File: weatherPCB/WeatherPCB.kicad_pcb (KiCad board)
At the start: 2 copper layers, 14 parts, among them Q1 2N4403-ND, Q2 2N4401-ND, SW1 SW_Push, SW2 SW_SPDT, U1 PIR_MTN_SNR, U2 WeMos_mini, U3 TFTLCD_ST7735R

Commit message: created pcb
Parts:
- C1: footprint Capacitors_THT:C_Axial_L3.8mm_D2.6mm_P7.50mm_Horizontal -> Capacitors_THT:C_Disc_D3.8mm_W2.6mm_P2.50mm
- moved R5 26.9 mm to (166.0, 139.7), turned to 0 degrees
- moved C1 21.2 mm to (168.9, 133.8), turned to 90 degrees
- moved R2 18.8 mm to (165.5, 132.0), turned to 270 degrees
- moved R1 18.2 mm to (153.5, 126.2), turned to 0 degrees
- moved U1 15.8 mm to (175.2, 135.3)
- moved U3 15.6 mm to (182.9, 92.2)
- moved R6 15.4 mm to (172.0, 135.9), turned to 90 degrees
- moved SW1 12.7 mm to (152.1, 135.6)
- moved U2 11.4 mm to (174.9, 116.5)
- moved R3 10.8 mm to (160.8, 126.2)
- moved Q1 9.48 mm to (160.0, 130.4)
- moved Q2 9.48 mm to (153.7, 130.4)
- moved SW2 6.08 mm to (170.8, 127.0)
- moved R4 2.40 mm to (161.8, 140.5)
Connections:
- U1 pad 1: +3V3 -> GND
- U1 pad 3: GND -> +3V3
- U2 pad 1: +5V -> (no net)
- U2 pad 10: Net-(C1-Pad1) -> GND
- U2 pad 11: Net-(U2-Pad11) -> (no net)
- U2 pad 12: Net-(U2-Pad12) -> Net-(R1-Pad2)
- U2 pad 13: Net-(U2-Pad13) -> Net-(U1-Pad2)
- U2 pad 14: Net-(U2-Pad14) -> Net-(R4-Pad1)
- U2 pad 15: Net-(U2-Pad15) -> (no net)
- U2 pad 16: +3V3 -> (no net)
- U2 pad 2: GND -> Net-(C1-Pad1)
- U2 pad 3: (no net) -> Net-(U2-Pad3)
- U2 pad 4: Net-(R1-Pad2) -> Net-(U2-Pad4)
- U2 pad 5: Net-(U1-Pad2) -> Net-(U2-Pad5)
- U2 pad 6: Net-(R4-Pad1) -> Net-(U2-Pad6)
- U2 pad 7: (no net) -> Net-(U2-Pad7)
- U2 pad 8: (no net) -> +3V3
- U2 pad 9: (no net) -> +5V
- U3 pad 10: Net-(U2-Pad15) -> Net-(U2-Pad7)
- U3 pad 6: Net-(U2-Pad13) -> Net-(U2-Pad5)
- U3 pad 7: Net-(U2-Pad11) -> Net-(U2-Pad3)
- U3 pad 8: Net-(U2-Pad14) -> Net-(U2-Pad6)
- U3 pad 9: Net-(U2-Pad12) -> Net-(U2-Pad4)
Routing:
- net Net-(U1-Pad2): track 0.00 -> 50.9 mm
- net +3V3: track 0.00 -> 44.8 mm, vias 0 -> 2
- net Net-(R4-Pad1): track 0.00 -> 43.1 mm
- net Net-(C1-Pad1): track 0.00 -> 37.1 mm
- net +5V: track 0.00 -> 35.0 mm
- net Net-(R1-Pad2): track 0.00 -> 23.3 mm, vias 0 -> 1
- net Net-(U2-Pad7): track 0.00 -> 18.0 mm, vias 0 -> 1
- net Net-(U2-Pad6): track 0.00 -> 11.9 mm
- net Net-(SW2-Pad2): track 0.00 -> 11.9 mm
- net Net-(Q1-Pad2): track 0.00 -> 10.8 mm
- net Net-(U2-Pad3): track 0.00 -> 9.69 mm
- net Net-(Q1-Pad3): track 0.00 -> 9.64 mm
- net Net-(U2-Pad4): track 0.00 -> 9.52 mm
- net Net-(U2-Pad5): track 0.00 -> 8.64 mm
- net Net-(Q2-Pad2): track 0.00 -> 4.81 mm
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- added copper zone on F.Cu, net +3V3
- added copper zone on B.Cu, net GND
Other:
- board outline added: 35 x 52 mm
- board text added: "Weather Station Miles Young"

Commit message: Rev 1 PCB finished
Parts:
- added H1: MountingHole, Mounting_Holes:MountingHole_2.7mm, F.Cu at (153.0, 93.0)
- added H2: MountingHole, Mounting_Holes:MountingHole_2.7mm, F.Cu at (178.0, 93.0)
- added H3: MountingHole, Mounting_Holes:MountingHole_2.7mm, F.Cu at (153.0, 133.0)
- added H4: MountingHole, Mounting_Holes:MountingHole_2.7mm, F.Cu at (178.0, 133.0)
- C1: footprint Capacitors_THT:C_Disc_D3.8mm_W2.6mm_P2.50mm -> Capacitors_THT:C_Disc_D3.0mm_W1.6mm_P2.50mm
- moved R6 7.42 mm to (166.6, 141.0)
- moved U1 5.82 mm to (169.9, 137.7)
- moved R5 5.75 mm to (161.6, 143.4)
- moved R4 4.88 mm to (161.8, 135.6), turned to 180 degrees
- moved R2 4.20 mm to (164.1, 135.9)
- moved Q2 3.10 mm to (156.8, 130.2)
- moved SW1 2.92 mm to (152.2, 138.5)
- moved Q1 2.34 mm to (162.4, 130.2)
- moved C1 1.92 mm to (167.0, 133.5), turned to 0 degrees
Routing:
- net Net-(R4-Pad1): track 43.1 -> 49.1 mm
- net Net-(U1-Pad2): track 50.9 -> 46.6 mm, vias 0 -> 2
- net Net-(C1-Pad1): track 37.1 -> 41.0 mm
- net +3V3: track 44.8 -> 47.1 mm, vias 2 -> 3
- net Net-(Q2-Pad2): track 4.81 -> 6.85 mm
- net Net-(Q1-Pad3): track 9.64 -> 7.90 mm
- net Net-(R2-Pad2): track 2.84 -> 4.15 mm
- net +5V: track 35.0 -> 34.1 mm
- net Net-(Q1-Pad2): track 10.8 -> 10.3 mm
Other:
- board size 35 x 52 mm -> 35 x 55 mm
- board text added: "JLCJLCJLCJLC"
- board text added: "Weather Station PCB v1 M Young"
- board text removed: "Weather Station Miles Young"

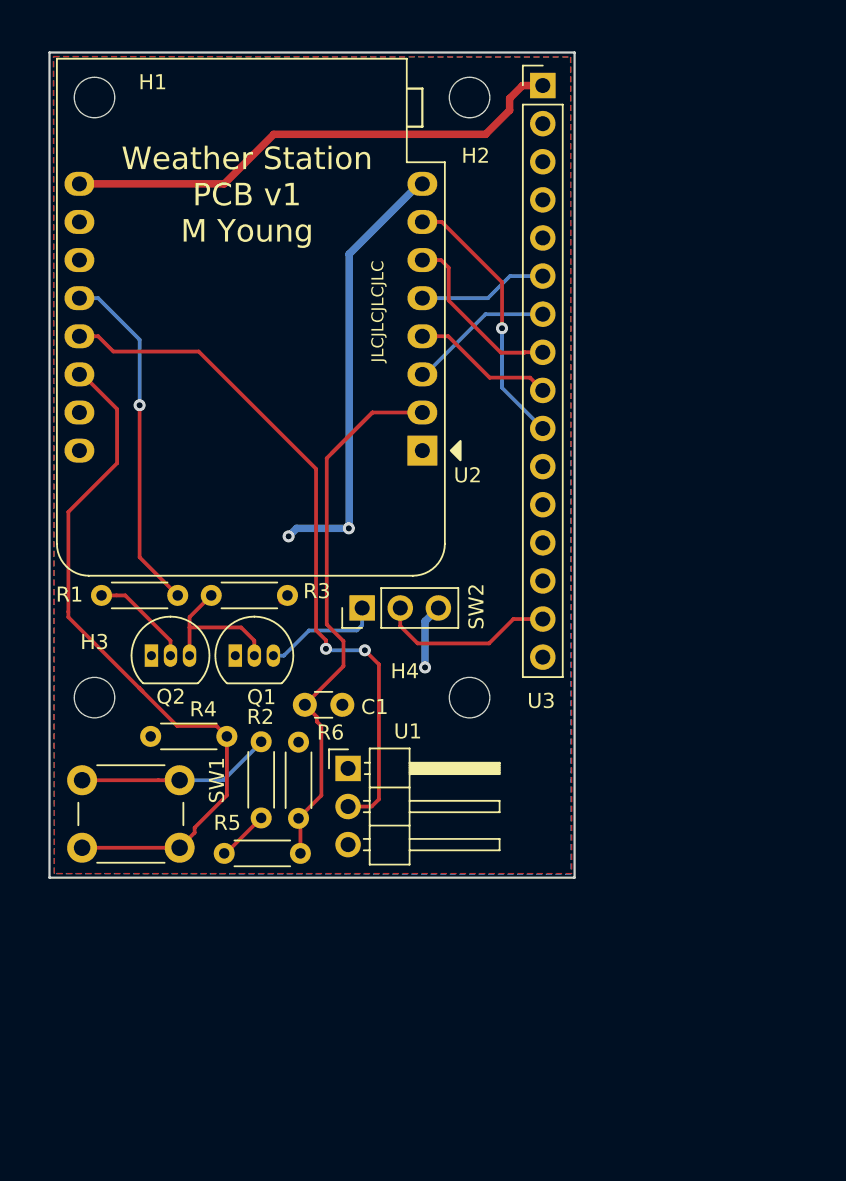
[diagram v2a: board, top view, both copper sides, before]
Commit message: Modified PCB for larger resistor sizes and KiCad error with display wiring
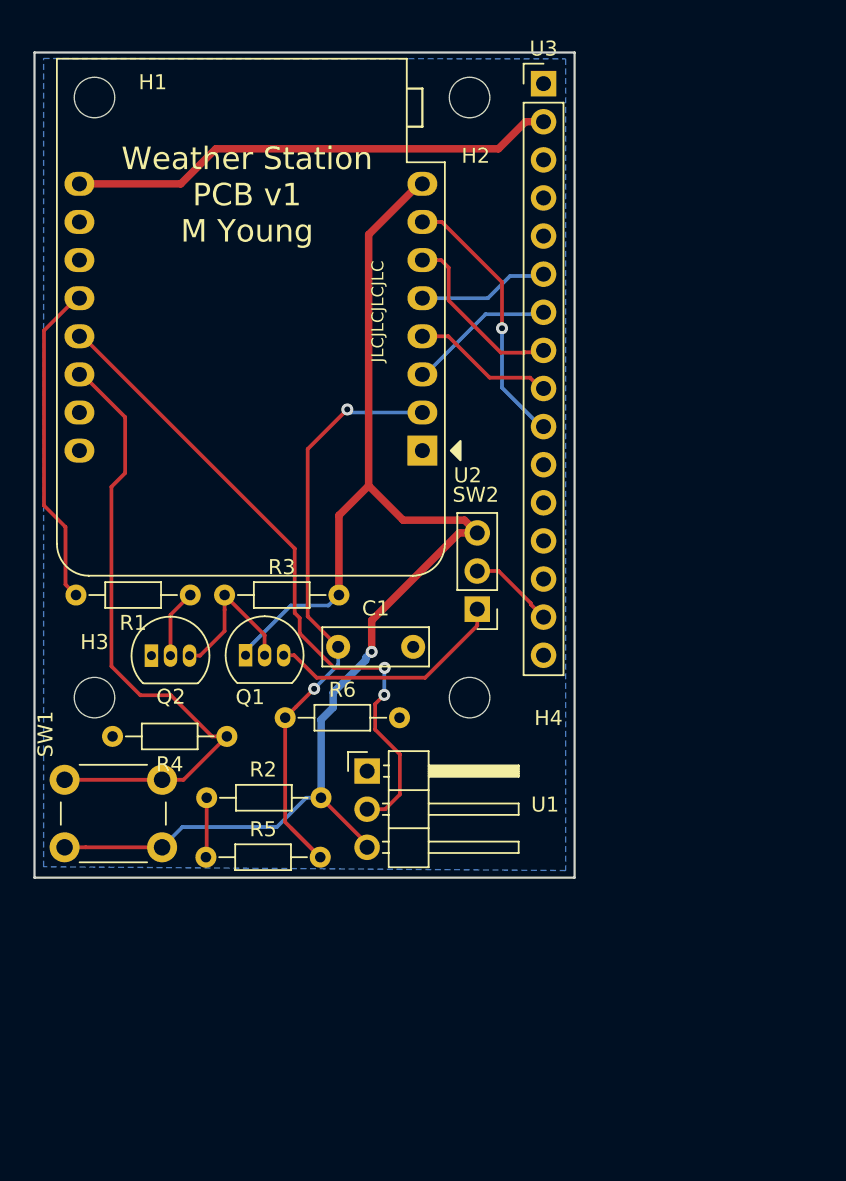
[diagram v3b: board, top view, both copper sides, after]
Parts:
- C1: footprint Capacitors_THT:C_Disc_D3.0mm_W1.6mm_P2.50mm -> Capacitors_THT:C_Disc_D7.0mm_W2.5mm_P5.00mm
- R1, R2, R3, R4, R5, R6: footprint Resistors_THT:R_Axial_DIN0204_L3.6mm_D1.6mm_P5.08mm_Horizontal -> Resistors_THT:R_Axial_DIN0204_L3.6mm_D1.6mm_P7.62mm_Horizontal
- moved SW2 7.67 mm to (178.5, 127.1), turned to 180 degrees
- moved SW1 6.96 mm to (157.5, 143.0), turned to 180 degrees
- moved R6 6.76 mm to (165.7, 134.3), turned to 0 degrees
- moved R1 5.92 mm to (159.4, 126.2), turned to 180 degrees
- moved R2 5.46 mm to (168.1, 139.7), turned to 180 degrees
- moved C1 4.45 mm to (169.2, 129.6)
- moved U1 1.28 mm to (171.2, 137.9)
- moved R5 1.25 mm to (160.4, 143.6)
- moved R3 0.89 mm to (161.7, 126.2)
- moved Q1 0.69 mm to (163.1, 130.2)
- moved U3 0.14 mm to (182.9, 92.1)
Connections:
- U3 pad 1: +5V -> GND
- U3 pad 2: GND -> +5V
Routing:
- net +3V3: track 47.1 -> 92.4 mm, vias 3 -> 1
- net Net-(Q1-Pad3): track 7.90 -> 16.1 mm
- net Net-(SW2-Pad2): track 11.9 -> 5.74 mm
- net Net-(R4-Pad1): track 49.1 -> 43.1 mm
- net Net-(Q2-Pad2): track 6.85 -> 4.59 mm
- net Net-(U1-Pad2): track 46.6 -> 44.6 mm
- net Net-(C1-Pad1): track 41.0 -> 42.7 mm, vias 0 -> 2
- net Net-(R1-Pad2): track 23.3 -> 21.8 mm, vias 1 -> 0
- net +5V: track 34.1 -> 32.7 mm
- removed copper zone on F.Cu, net +3V3
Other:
- board size 35 x 55 mm -> 36 x 55 mm

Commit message: Added space for optional 1-wire temp sensor
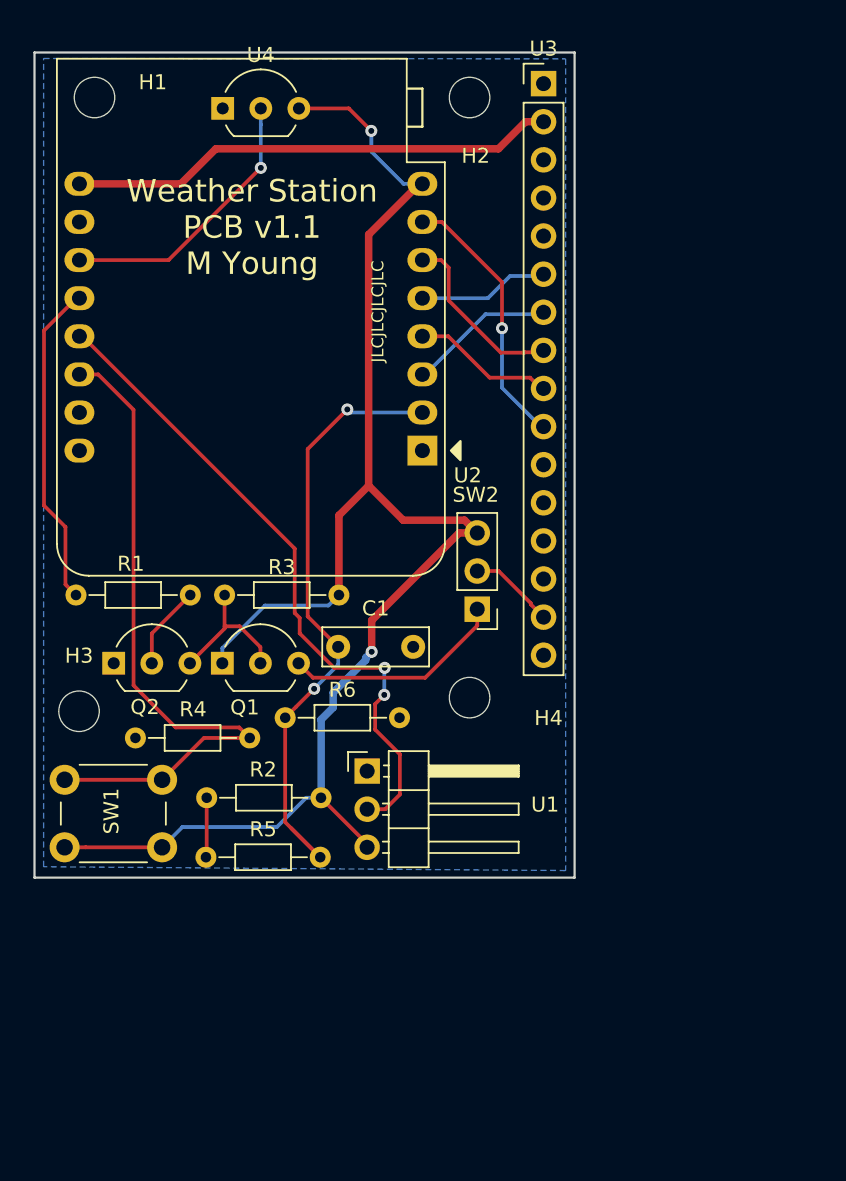
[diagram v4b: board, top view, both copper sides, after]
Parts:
- added U4: DS1822, TO_SOT_Packages_THT:TO-92_Inline_Wide, F.Cu at (161.5, 93.7)
- Q1, Q2: footprint TO_SOT_Packages_THT:TO-92_Inline_Narrow_Oval -> TO_SOT_Packages_THT:TO-92_Inline_Wide
- moved Q2 2.57 mm to (154.3, 130.7)
- moved Q1 1.64 mm to (161.5, 130.7)
- moved R4 1.53 mm to (163.3, 135.7)
- moved H3 1.37 mm to (152.0, 133.9)
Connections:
- U2 pad 11: (no net) -> Net-(U2-Pad11)
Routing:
- net Net-(U2-Pad11): track 0.00 -> 18.6 mm, vias 0 -> 1
- net +3V3: track 92.4 -> 105.7 mm, vias 1 -> 2
- net Net-(R4-Pad1): track 43.1 -> 45.6 mm
- net Net-(Q1-Pad3): track 16.1 -> 14.9 mm
- net Net-(Q2-Pad2): track 4.59 -> 5.61 mm
- net Net-(Q1-Pad2): track 10.5 -> 9.54 mm
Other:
- board text added: "Weather Station PCB v1.1 M Young"
- board text removed: "Weather Station PCB v1 M Young"
